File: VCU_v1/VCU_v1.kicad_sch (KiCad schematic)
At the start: 0 parts

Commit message: began designing power schem
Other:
- added sheet Power (power.kicad_sch)
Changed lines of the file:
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@@
+		)
+	)
+	(sheet
+		(at 53.34 59.69)
+		(size 20.955 7.62)
+		(exclude_from_sim no)
+		(in_bom yes)
+		(on_board yes)
+		(dnp no)
+		(fields_autoplaced yes)
+		(stroke
+			(width 0.1524)
+			(type solid)
+		)
+		(fill
+			(color 0 0 0 0.0000)
+		)
+		(property "Sheetname" "Power"
+			(at 53.34 58.9784 0)
+			(effects
+				(font
+					(size 1.27 1.27)
+				)
+				(justify left bottom)
+			)
+		)
+		(property "Sheetfile" "power.kicad_sch"
+			(at 53.34 67.8946 0)
+			(effects
+				(font
+					(size 1.27 1.27)
+				)
+				(justify left top)
+			)
+		)
+		(instances
+			(project "VCU_v1"
+				(path "/4ee6c2ad-9a1b-4276-b3cf-1cc8dc52967e"
+					(page "2")
+				)
+			)
 		)
 	)

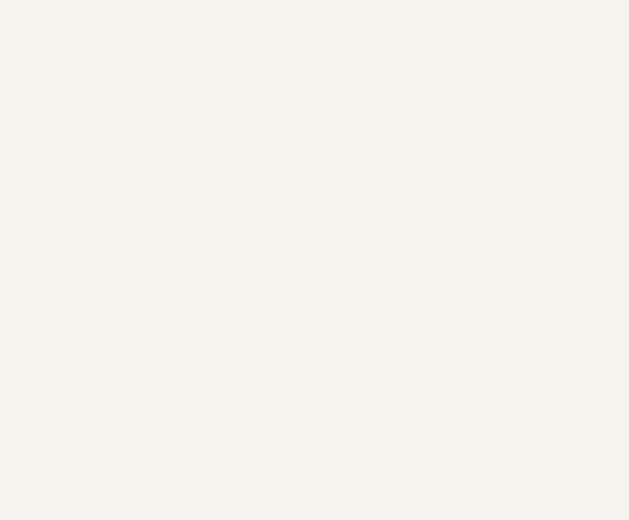
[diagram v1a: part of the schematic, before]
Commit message: finished 12-5 buck
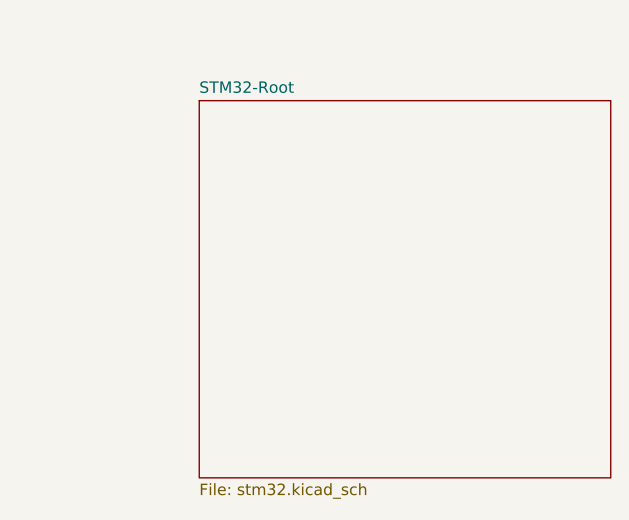
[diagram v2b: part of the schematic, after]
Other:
- added sheet STM32-Root (stm32.kicad_sch)
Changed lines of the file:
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@@
+		)
+	)
+	(sheet
+		(at 118.11 60.96)
+		(size 45.72 41.91)
+		(exclude_from_sim no)
+		(in_bom yes)
+		(on_board yes)
+		(dnp no)
+		(fields_autoplaced yes)
+		(stroke
+			(width 0.1524)
+			(type solid)
+		)
+		(fill
+			(color 0 0 0 0.0000)
+		)
+		(property "Sheetname" "STM32-Root"
+			(at 118.11 60.2484 0)
+			(effects
+				(font
+					(size 1.27 1.27)
+				)
+				(justify left bottom)
+			)
+		)
+		(property "Sheetfile" "stm32.kicad_sch"
+			(at 118.11 103.4546 0)
+			(effects
+				(font
+					(size 1.27 1.27)
+				)
+				(justify left top)
+			)
+		)
+		(instances
+			(project "VCU_v1"
+				(path "/4ee6c2ad-9a1b-4276-b3cf-1cc8dc52967e"
+					(page "4")
+				)
+			)
 		)
 	)

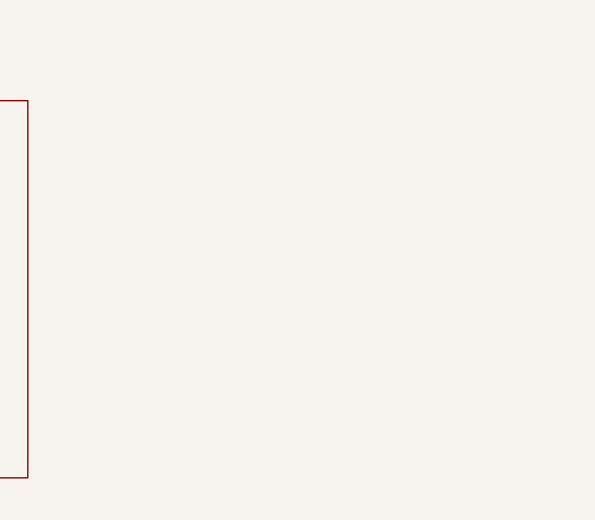
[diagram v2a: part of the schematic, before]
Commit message: added rpp, pedal buffer/low pass, can transceivers, began connector pinout
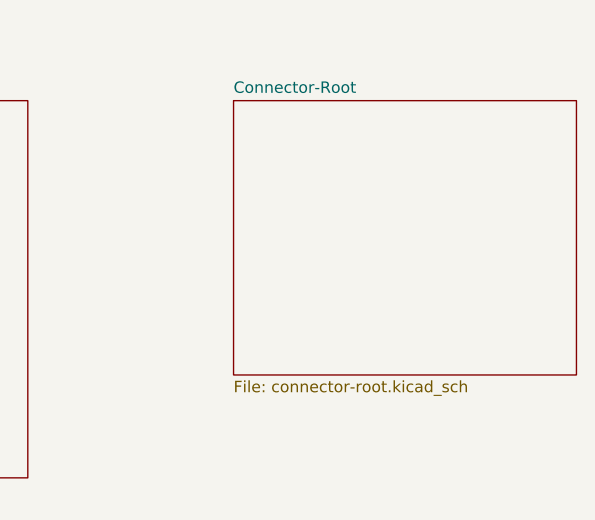
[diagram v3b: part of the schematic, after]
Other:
- added sheet Connector-Root (connector-root.kicad_sch)
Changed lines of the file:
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@@
+	)
+	(sheet
+		(at 186.69 60.96)
+		(size 38.1 30.48)
+		(exclude_from_sim no)
+		(in_bom yes)
+		(on_board yes)
+		(dnp no)
+		(fields_autoplaced yes)
+		(stroke
+			(width 0.1524)
+			(type solid)
+		)
+		(fill
+			(color 0 0 0 0.0000)
+		)
+		(property "Sheetname" "Connector-Root"
+			(at 186.69 60.2484 0)
+			(effects
+				(font
+					(size 1.27 1.27)
+				)
+				(justify left bottom)
+			)
+		)
+		(property "Sheetfile" "connector-root.kicad_sch"
+			(at 186.69 92.0246 0)
+			(effects
+				(font
+					(size 1.27 1.27)
+				)
+				(justify left top)
+			)
+		)
+		(instances
+			(project "VCU_v1"
+				(path "/4ee6c2ad-9a1b-4276-b3cf-1cc8dc52967e"
+					(page "8")
+				)
+			)
+		)
 	)
 	(sheet

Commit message: p dih r
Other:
- sheet Connector-Root ports: added APPS1-4.8V, APPS1-GND, APPS1-SIG, APPS2-4.8V, APPS2-GND, APPS2-SIG, BMS-FAULT, BMS_FAULT+, BMS_FAULT-, BRAKE_LIGHT, BSE-4.8V, BSE-GND, BSE-SIG, BSPD-FAULT, BSPD_FAULT+, BSPD_FAULT-, GEN_BTN1+, GEN_BTN1-, GEN_BTN2+, GEN_BTN2-, GEN_DB2+, GEN_DB2-, GEN_DB3+, GEN_DB3-, IMD-FAULT, IMD_FAULT+, IMD_FAULT-, PRECHARGE_BTN+, PRECHARGE_BTN-, RTD_BTN+, RTD_BTN-, SPEAKER+, SPEAKER-, uSD_CLK, uSD_CMD, uSD_D0, uSD_D1, uSD_D2, uSD_D3; removed none
- sheet Power ports: added VBAT+; removed none
- sheet STM32-Root ports: added APPS1-SIG, APPS2-SIG, BMS-FAULT, BMS_LED+, BMS_LED-, BRAKE-LIGHT, BSE-SIG, BSPD-FAULT, BSPD_LED+, BSPD_LED-, BT1_T1, BT1_T2, BT2_T1, BT2_T2, BT3_T1, BT3_T2, BT4_T1, BT4_T2, CAN1_H, CAN1_L, CAN2_H, CAN2_L, CAN3_H, CAN3_L, IMD-FAULT, IMD_LED+, IMD_LED-, SD_CK, SD_CMD, SD_D0, SD_D1, SD_D2, SD_D3, SPEAKER+, SPEAKER-; removed none

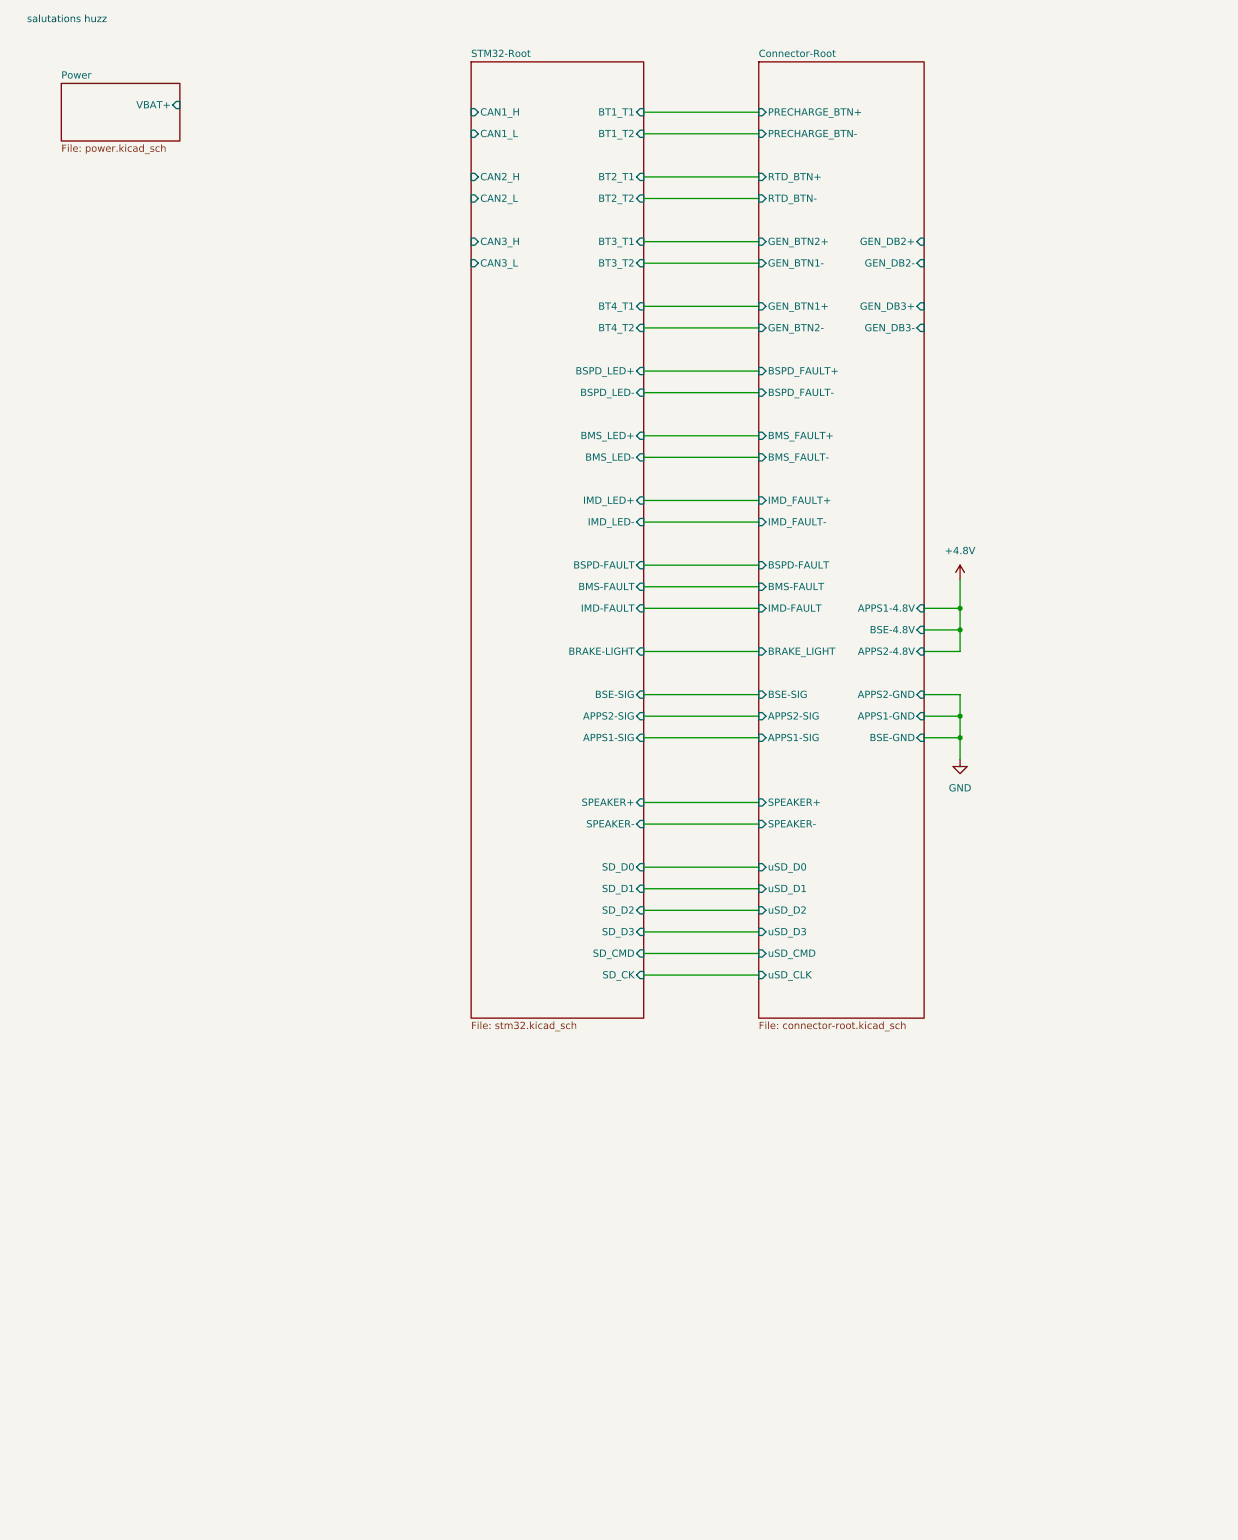
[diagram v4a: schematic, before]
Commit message: v1 schematic (actually) complete, let the layout commence
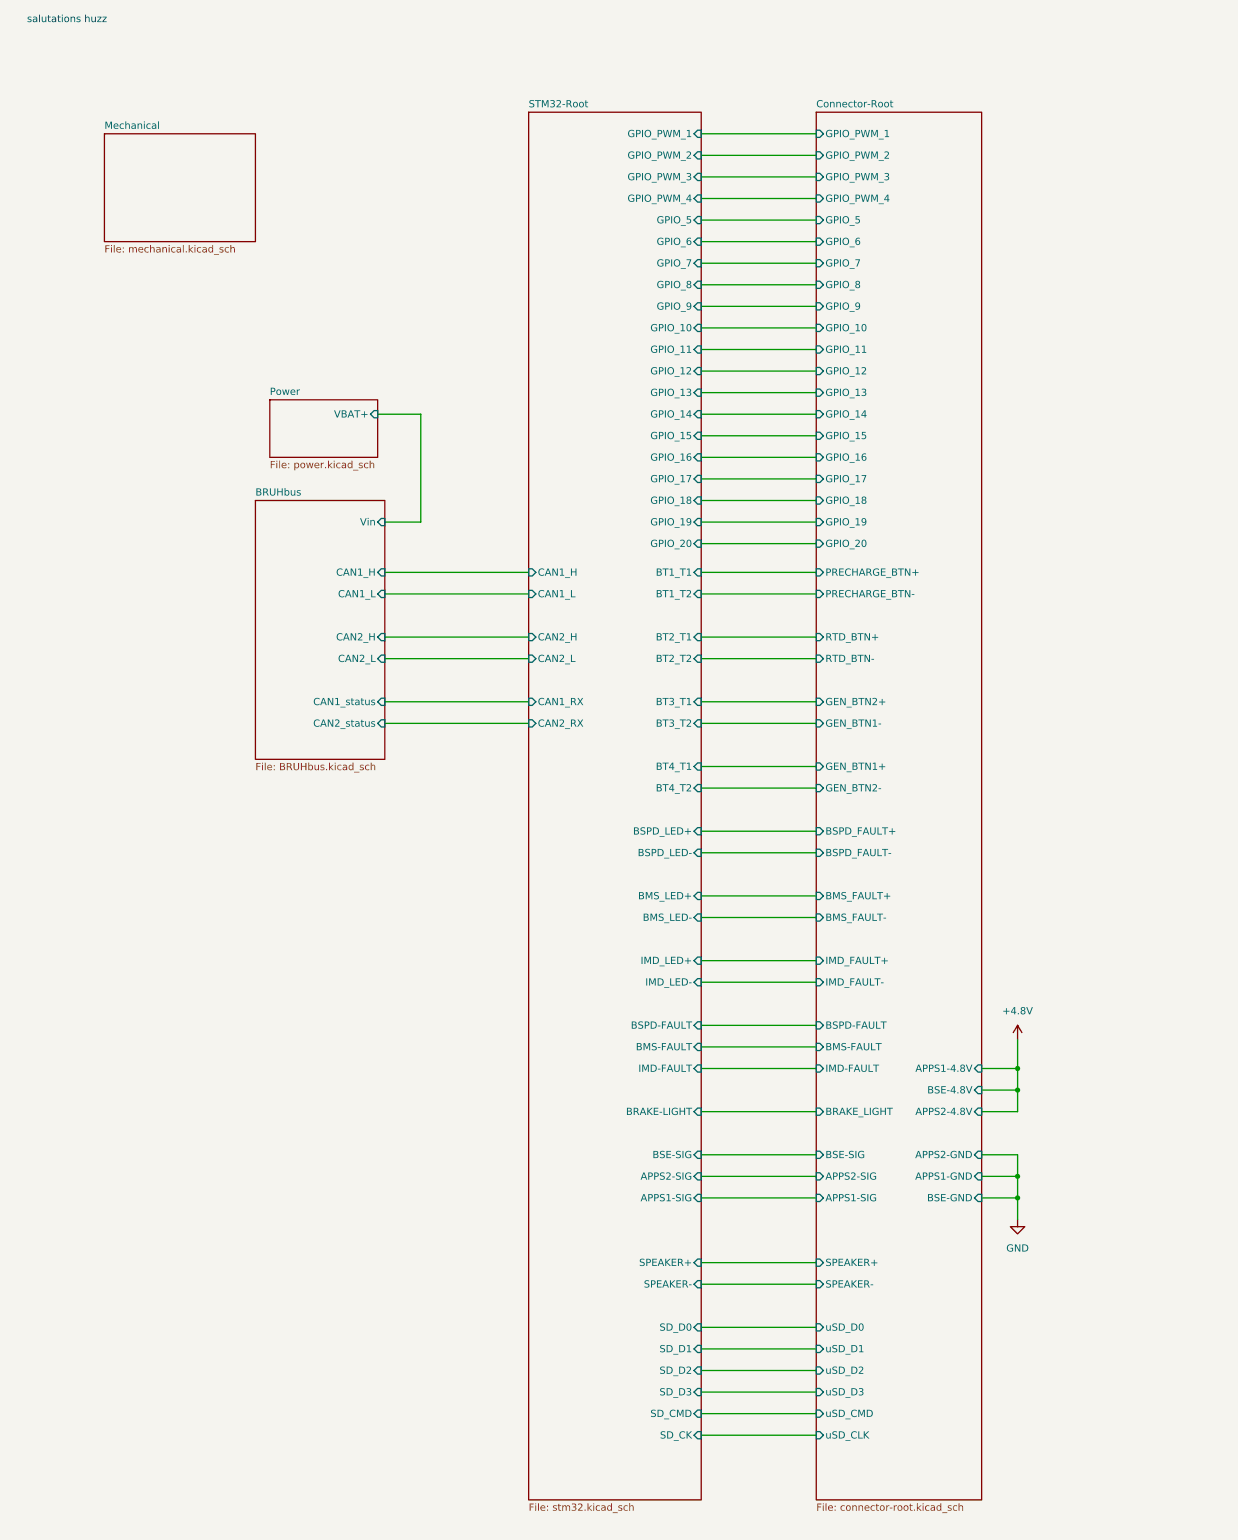
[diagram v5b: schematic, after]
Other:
- added sheet BRUHbus (BRUHbus.kicad_sch)
- added sheet Mechanical (mechanical.kicad_sch)
- sheet Connector-Root ports: added GPIO_10, GPIO_11, GPIO_12, GPIO_13, GPIO_14, GPIO_15, GPIO_16, GPIO_17, GPIO_18, GPIO_19, GPIO_20, GPIO_5, GPIO_6, GPIO_7, GPIO_8, GPIO_9, GPIO_PWM_1, GPIO_PWM_2, GPIO_PWM_3, GPIO_PWM_4; removed GEN_DB2+, GEN_DB2-, GEN_DB3+, GEN_DB3-
- sheet STM32-Root ports: added CAN1_RX, CAN2_RX, GPIO_10, GPIO_11, GPIO_12, GPIO_13, GPIO_14, GPIO_15, GPIO_16, GPIO_17, GPIO_18, GPIO_19, GPIO_20, GPIO_5, GPIO_6, GPIO_7, GPIO_8, GPIO_9, GPIO_PWM_1, GPIO_PWM_2, GPIO_PWM_3, GPIO_PWM_4; removed CAN3_H, CAN3_L

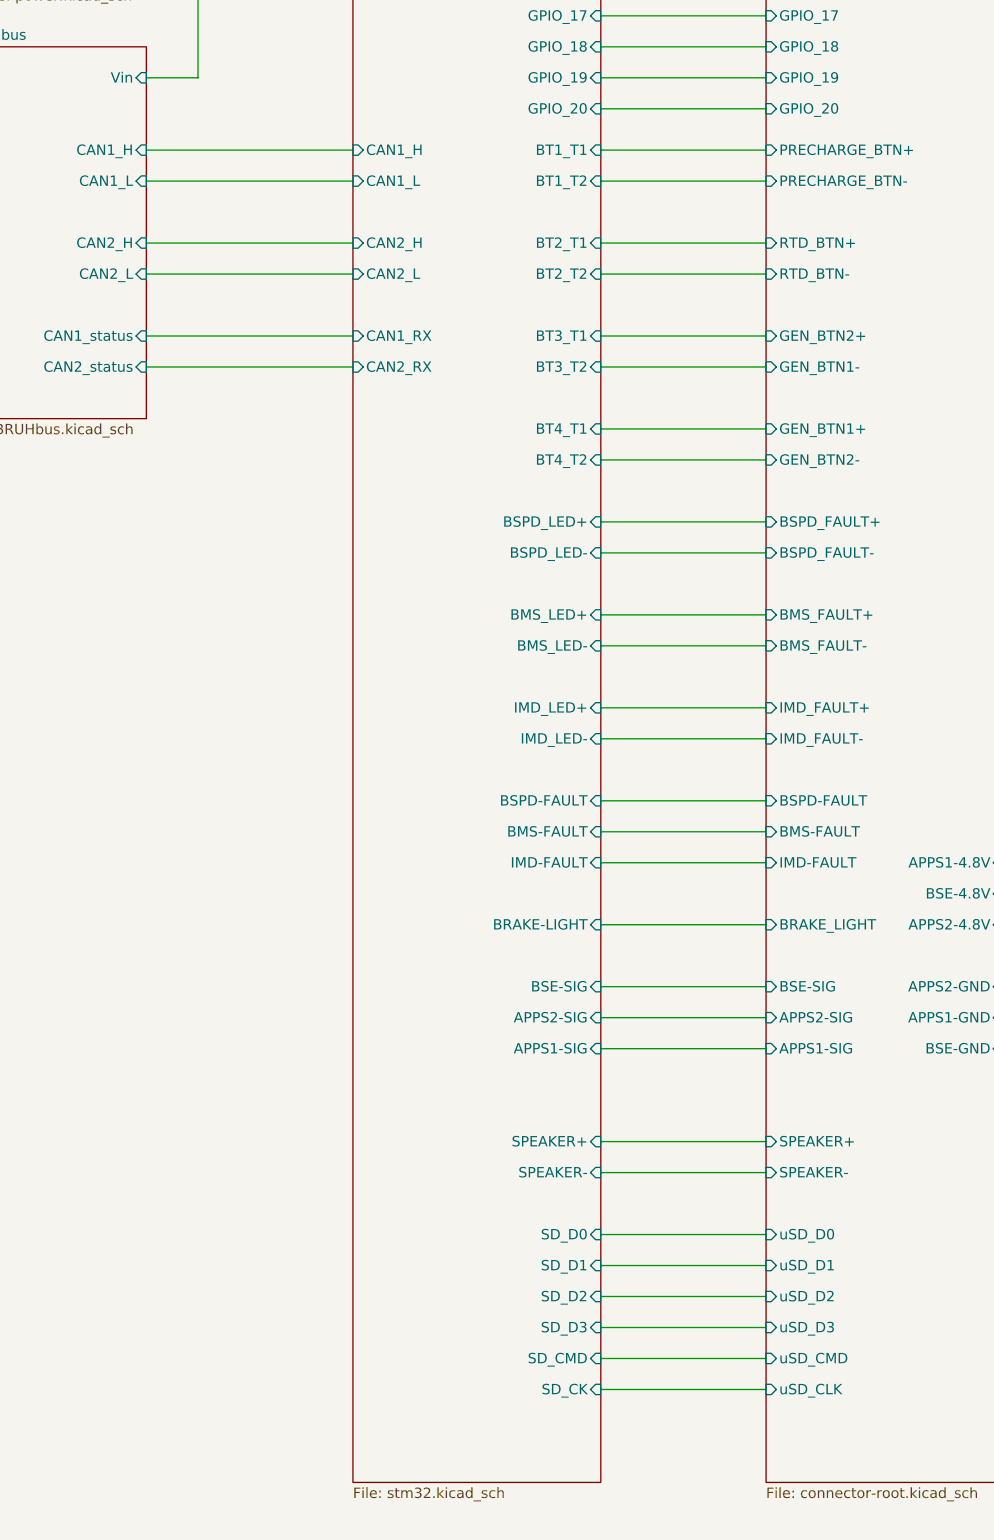
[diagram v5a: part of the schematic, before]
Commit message: vcu placements complete
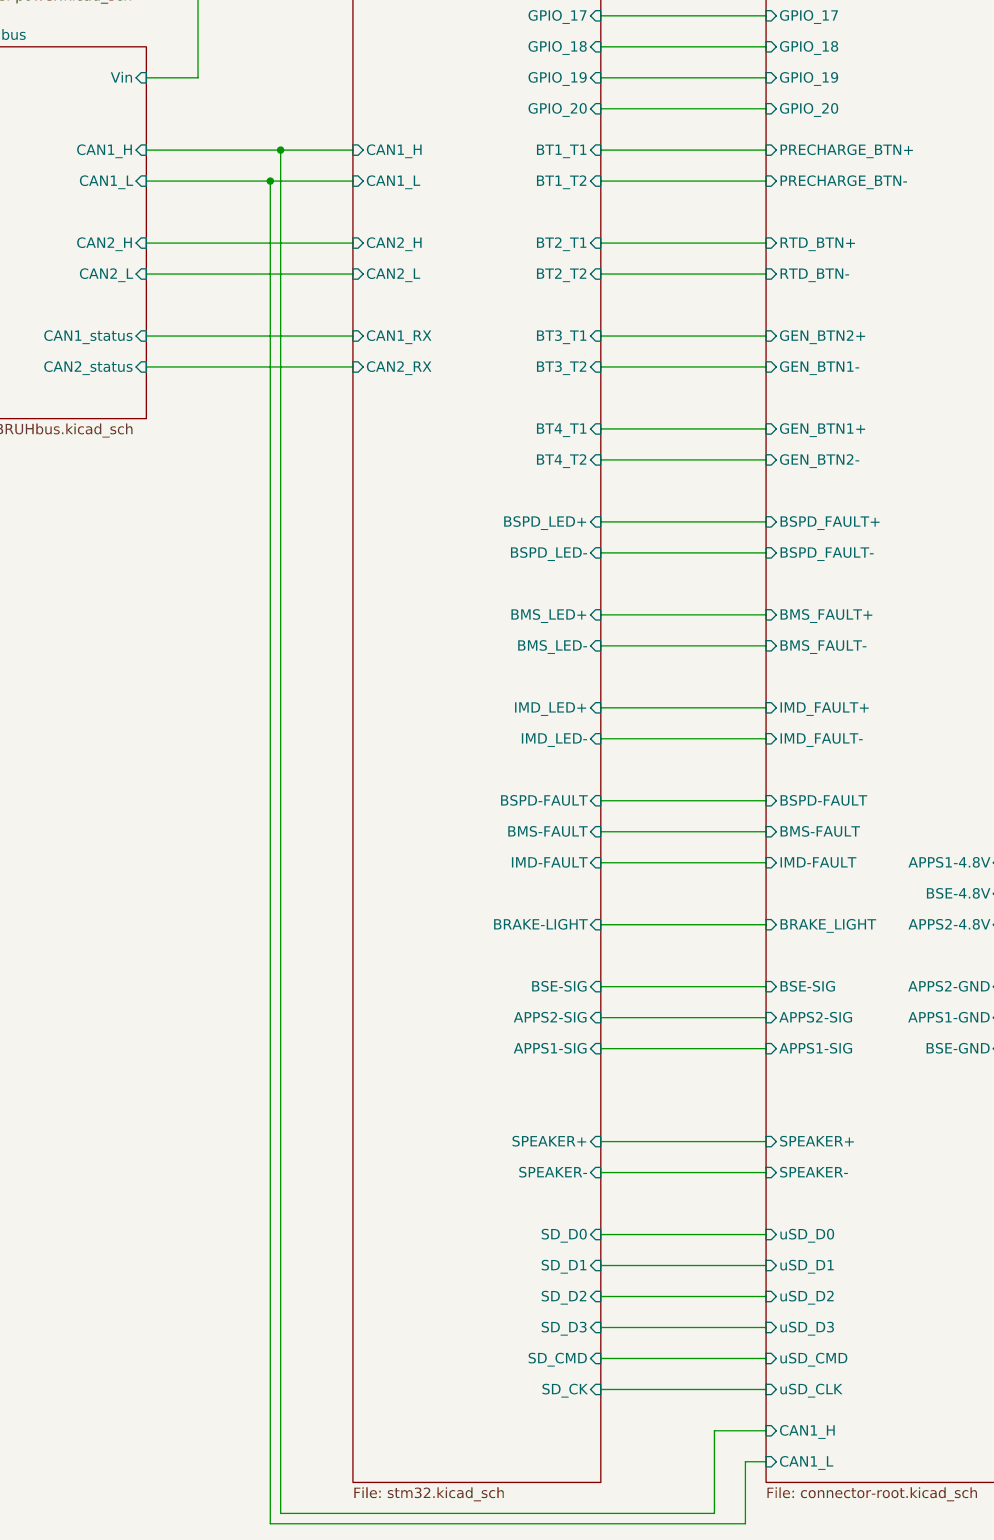
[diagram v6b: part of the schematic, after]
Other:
- sheet Connector-Root ports: added CAN1_H, CAN1_L; removed none
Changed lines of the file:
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@@
+	)
+	(junction
+		(at 92.71 111.76)
+		(diameter 0)
+		(color 0 0 0 0)
 	)
 	(junction
@@
 	)
 	(junction
+		(at 91.44 115.57)
+		(diameter 0)
+		(color 0 0 0 0)
+	)
+	(junction
 		(at 187.96 222.25)
 		(diameter 0)
@@
 	(wire
 		(pts
-			(xy 76.2 115.57) (xy 101.6 115.57)
+			(xy 76.2 115.57) (xy 91.44 115.57)
 		)
 		(stroke
@@
 	(wire
 		(pts
+			(xy 146.05 269.24) (xy 146.05 279.4)
+		)
+		(stroke
+			(width 0)
+			(type default)
+		)
+	)
+	(wire
+		(pts
 			(xy 82.55 83.82) (xy 82.55 102.87)
 		)
@@
 	(wire
 		(pts
+			(xy 92.71 111.76) (xy 101.6 111.76)
+		)
+		(stroke
+			(width 0)
+			(type default)
+		)
+	)
+	(wire
+		(pts
 			(xy 132.08 127) (xy 152.4 127)
 		)
@@
 	(wire
 		(pts
+			(xy 92.71 279.4) (xy 92.71 111.76)
+		)
+		(stroke
+			(width 0)
+			(type default)
+		)
+	)
+	(wire
+		(pts
 			(xy 132.08 207.01) (xy 152.4 207.01)
 		)
@@
 	(wire
 		(pts
+			(xy 152.4 269.24) (xy 146.05 269.24)
+		)
+		(stroke
+			(width 0)
+			(type default)
+		)
+	)
+	(wire
+		(pts
 			(xy 132.08 72.39) (xy 152.4 72.39)
 		)
@@
 	(wire
 		(pts
+			(xy 91.44 280.67) (xy 91.44 115.57)
+		)
+		(stroke
+			(width 0)
+			(type default)
+		)
+	)
+	(wire
+		(pts
 			(xy 132.08 34.29) (xy 152.4 34.29)
 		)
@@
 	(wire
 		(pts
+			(xy 152.4 273.05) (xy 149.86 273.05)
+		)
+		(stroke
+			(width 0)
+			(type default)
+		)
+	)
+	(wire
+		(pts
 			(xy 132.08 106.68) (xy 152.4 106.68)
 		)
@@
 	(wire
 		(pts
+			(xy 149.86 280.67) (xy 91.44 280.67)
+		)
+		(stroke
+			(width 0)
+			(type default)
+		)
+	)
+	(wire
+		(pts
 			(xy 132.08 80.01) (xy 152.4 80.01)
 		)
@@
 	(wire
 		(pts
-			(xy 76.2 111.76) (xy 101.6 111.76)
+			(xy 76.2 111.76) (xy 92.71 111.76)
 		)
 		(stroke
@@
 	(wire
 		(pts
+			(xy 149.86 273.05) (xy 149.86 280.67)
+		)
+		(stroke
+			(width 0)
+			(type default)
+		)
+	)
+	(wire
+		(pts
 			(xy 132.08 195.58) (xy 152.4 195.58)
 		)
@@
 		(pts
 			(xy 181.61 199.39) (xy 187.96 199.39)
+		)
+		(stroke
+			(width 0)
+			(type default)
+		)
+	)
+	(wire
+		(pts
+			(xy 146.05 279.4) (xy 92.71 279.4)
+		)
+		(stroke
+			(width 0)
+			(type default)
+		)
+	)
+	(wire
+		(pts
+			(xy 91.44 115.57) (xy 101.6 115.57)
 		)
 		(stroke
@@
 			(effects
 				(font
+					(size 1.27 1.27)
+				)
+				(justify left)
+			)
+		)
+		(pin "CAN1_H" input
+			(at 152.4 269.24 180)
+			(effects
+				(font
+					(size 1.27 1.27)
+				)
+				(justify left)
+			)
+		)
+		(pin "CAN1_L" input
+			(at 152.4 273.05 180)
+			(effects
+				(font
